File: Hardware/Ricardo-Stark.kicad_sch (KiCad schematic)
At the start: 40 parts, among them J1 RBUS, U1 ESP32-S3, Y1 R940000171

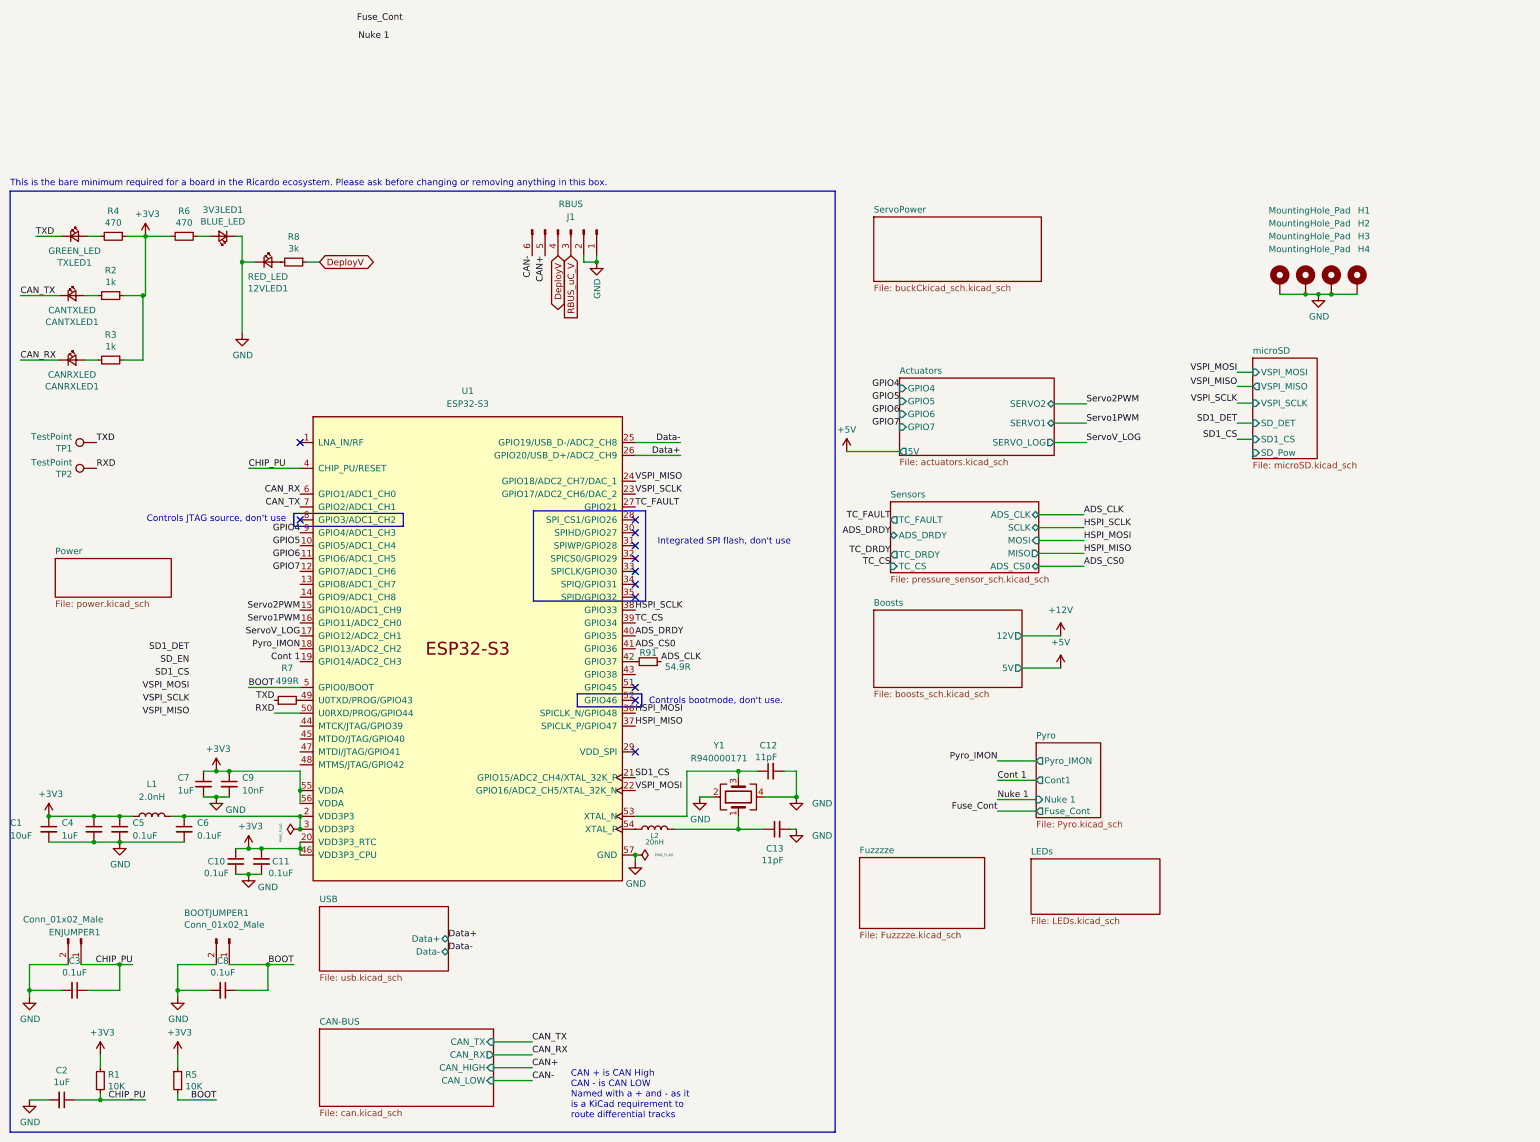
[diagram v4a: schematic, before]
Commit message: Routed Switch and Servo driver subsystems
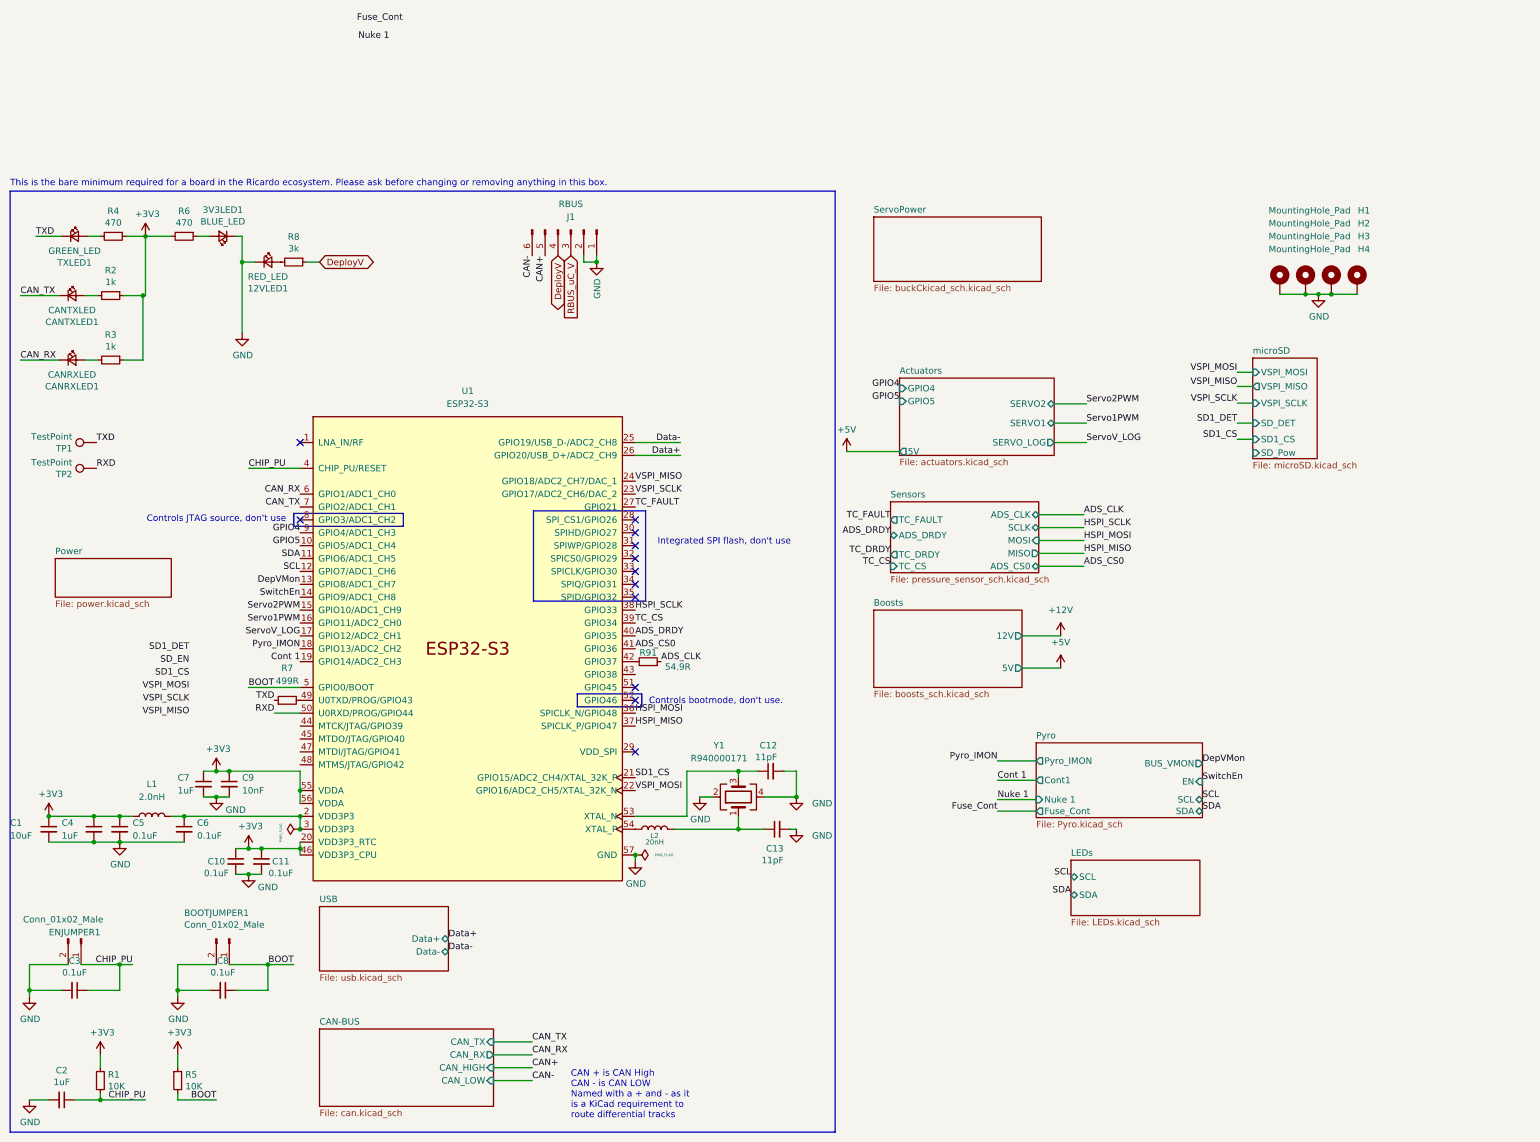
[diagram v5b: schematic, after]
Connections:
- net DepVMon: now reaches U1.13 (GPIO8/ADC1_CH7)
- net SwitchEn: now reaches U1.14 (GPIO9/ADC1_CH8)
- net GPIO6 renamed SDA
- net GPIO7 renamed SCL
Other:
- removed sheet Fuzzzze
- sheet Actuators ports: added none; removed GPIO6, GPIO7
- sheet LEDs ports: added SCL, SDA; removed none
- sheet Pyro ports: added BUS_VMON, EN, SCL, SDA; removed none
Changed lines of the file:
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@@
 		)
 	)
+	(label "SwitchEn"
+		(at 247.65 129.032 0)
+		(effects
+			(font
+				(size 1.27 1.27)
+			)
+			(justify left bottom)
+		)
+	)
 	(label "Nuke 1"
 		(at 207.264 132.588 0)
@@
 		)
 	)
+	(label "DepVMon"
+		(at 69.85 90.17 180)
+		(effects
+			(font
+				(size 1.27 1.27)
+			)
+			(justify right bottom)
+		)
+	)
 	(label "GPIO4"
 		(at 187.96 51.562 180)
@@
 		)
 	)
+	(label "SCL"
+		(at 247.65 132.588 0)
+		(effects
+			(font
+				(size 1.27 1.27)
+			)
+			(justify left bottom)
+		)
+	)
 	(label "VSPI_MISO"
 		(at 135.89 69.85 0)
@@
 		)
 	)
+	(label "SCL"
+		(at 221.742 147.828 180)
+		(effects
+			(font
+				(size 1.27 1.27)
+			)
+			(justify right bottom)
+		)
+	)
 	(label "HSPI_SCLK"
 		(at 135.89 95.25 0)
@@
 		)
 	)
-	(label "GPIO7"
-		(at 187.96 59.182 180)
-		(effects
-			(font
-				(size 1.27 1.27)
-			)
-			(justify right bottom)
-		)
-	)
 	(label "Data-"
 		(at 99.06 162.56 0)
@@
 		)
 	)
+	(label "SDA"
+		(at 221.742 151.384 180)
+		(effects
+			(font
+				(size 1.27 1.27)
+			)
+			(justify right bottom)
+		)
+	)
 	(label "TC_DRDY"
 		(at 186.182 84.328 180)
@@
 		)
 	)
+	(label "SDA"
+		(at 69.85 85.09 180)
+		(effects
+			(font
+				(size 1.27 1.27)
+			)
+			(justify right bottom)
+		)
+	)
 	(label "TC_FAULT"
 		(at 135.89 74.93 0)
@@
 		)
 	)
+	(label "SwitchEn"
+		(at 69.85 92.71 180)
+		(effects
+			(font
+				(size 1.27 1.27)
+			)
+			(justify right bottom)
+		)
+	)
 	(label "CAN_TX"
 		(at 14.732 33.274 0)
@@
 		)
 	)
+	(label "SCL"
+		(at 69.85 87.63 180)
+		(effects
+			(font
+				(size 1.27 1.27)
+			)
+			(justify right bottom)
+		)
+	)
 	(label "SD1_DET"
 		(at 254.508 58.42 180)
@@
 		)
 	)
-	(label "GPIO7"
-		(at 69.85 87.63 180)
-		(effects
-			(font
-				(size 1.27 1.27)
-			)
-			(justify right bottom)
-		)
-	)
 	(label "VSPI_SCLK"
 		(at 254.508 54.483 180)
@@
 		)
 	)
-	(label "GPIO6"
-		(at 187.96 56.642 180)
+	(label "ServoV_LOG"
+		(at 224.79 62.23 0)
 		(effects
 			(font
 				(size 1.27 1.27)
 			)
-			(justify right bottom)
+			(justify left bottom)
 		)
 	)
-	(label "ServoV_LOG"
-		(at 224.79 62.23 0)
+	(label "VSPI_MOSI"
+		(at 135.89 130.81 0)
 		(effects
 			(font
@@
 		)
 	)
-	(label "VSPI_MOSI"
-		(at 135.89 130.81 0)
+	(label "DepVMon"
+		(at 247.65 125.476 0)
 		(effects
 			(font
@@
 		)
 	)
-	(label "GPIO6"
-		(at 69.85 85.09 180)
+	(label "SDA"
+		(at 247.65 134.874 0)
 		(effects
 			(font
 				(size 1.27 1.27)
 			)
-			(justify right bottom)
+			(justify left bottom)
 		)
 	)
@@
 	(sheet
 		(at 214.884 121.412)
-		(size 12.7 14.732)
+		(size 32.766 14.732)
 		(exclude_from_sim no)
 		(in_bom yes)
@@
 			)
 		)
+		(pin "BUS_VMON" output
+			(at 247.65 125.476 0)
+			(effects
+				(font
+					(size 1.27 1.27)
+				)
+				(justify right)
+			)
+		)
+		(pin "EN" input
+			(at 247.65 129.032 0)
+			(effects
+				(font
+					(size 1.27 1.27)
+				)
+				(justify right)
+			)
+		)
+		(pin "SCL" bidirectional
+			(at 247.65 132.588 0)
+			(effects
+				(font
+					(size 1.27 1.27)
+				)
+				(justify right)
+			)
+		)
+		(pin "SDA" bidirectional
+			(at 247.65 134.874 0)
+			(effects
+				(font
+					(size 1.27 1.27)
+				)
+				(justify right)
+			)
+		)
 		(instances
 			(project "Ricardo-Stark"
@@
 	)
 	(sheet
-		(at 213.868 144.272)
+		(at 221.742 144.526)
 		(size 25.4 10.922)
 		(exclude_from_sim no)
@@
 		)
 		(property "Sheetname" "LEDs"
-			(at 213.868 143.5604 0)
+			(at 221.742 143.8144 0)
 			(effects
 				(font
@@
 		)
 		(property "Sheetfile" "LEDs.kicad_sch"
-			(at 213.868 155.7786 0)
+			(at 221.742 156.0326 0)
 			(effects
 				(font
@@
 			)
 		)
+		(pin "SCL" bidirectional
+			(at 221.742 147.828 180)
+			(effects
+				(font
+					(size 1.27 1.27)
+				)
+				(justify left)
+			)
+		)
+		(pin "SDA" bidirectional
+			(at 221.742 151.384 180)
+			(effects
+				(font
+					(size 1.27 1.27)
+				)
+				(justify left)
+			)
+		)
 		(instances
 			(project "Ricardo-Stark"
@@
 			)
 		)
-		(pin "GPIO6" input
-			(at 187.96 56.642 180)
-			(effects
-				(font
-					(size 1.27 1.27)
-				)
-				(justify left)
-			)
-		)
-		(pin "GPIO7" input
-			(at 187.96 59.182 180)
-			(effects
-				(font
-					(size 1.27 1.27)
-				)
-				(justify left)
-			)
-		)
 		(instances
 			(project "Ricardo-Stark"
@@
 				)
 			)
-		)
-	)
-	(sheet
-		(at 180.086 144.018)
-		(size 24.638 13.97)
-		(exclude_from_sim no)
-		(in_bom yes)
-		(on_board yes)
-		(dnp no)
-		(fields_autoplaced yes)
-		(stroke
-			(width 0.1524)
-			(type solid)
-		)
-		(fill
-			(color 0 0 0 0.0000)
-		)
-		(property "Sheetname" "Fuzzzze"
-			(at 180.086 143.3064 0)
-			(effects
-				(font
-					(size 1.27 1.27)
-				)
-				(justify left bottom)
-			)
-		)
-		(property "Sheetfile" "Fuzzzze.kicad_sch"
-			(at 180.086 158.5726 0)
-			(effects
-				(font
-					(size 1.27 1.27)
-				)
-				(justify left top)
-			)
-		)
-		(instances
-			(project "Ricardo-Stark"
-				(path "/7db990e4-92e1-4f99-b4d2-435bbec1ba83"
-					(page "12")
-				)
-			)

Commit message: Added actuators and I2C bus
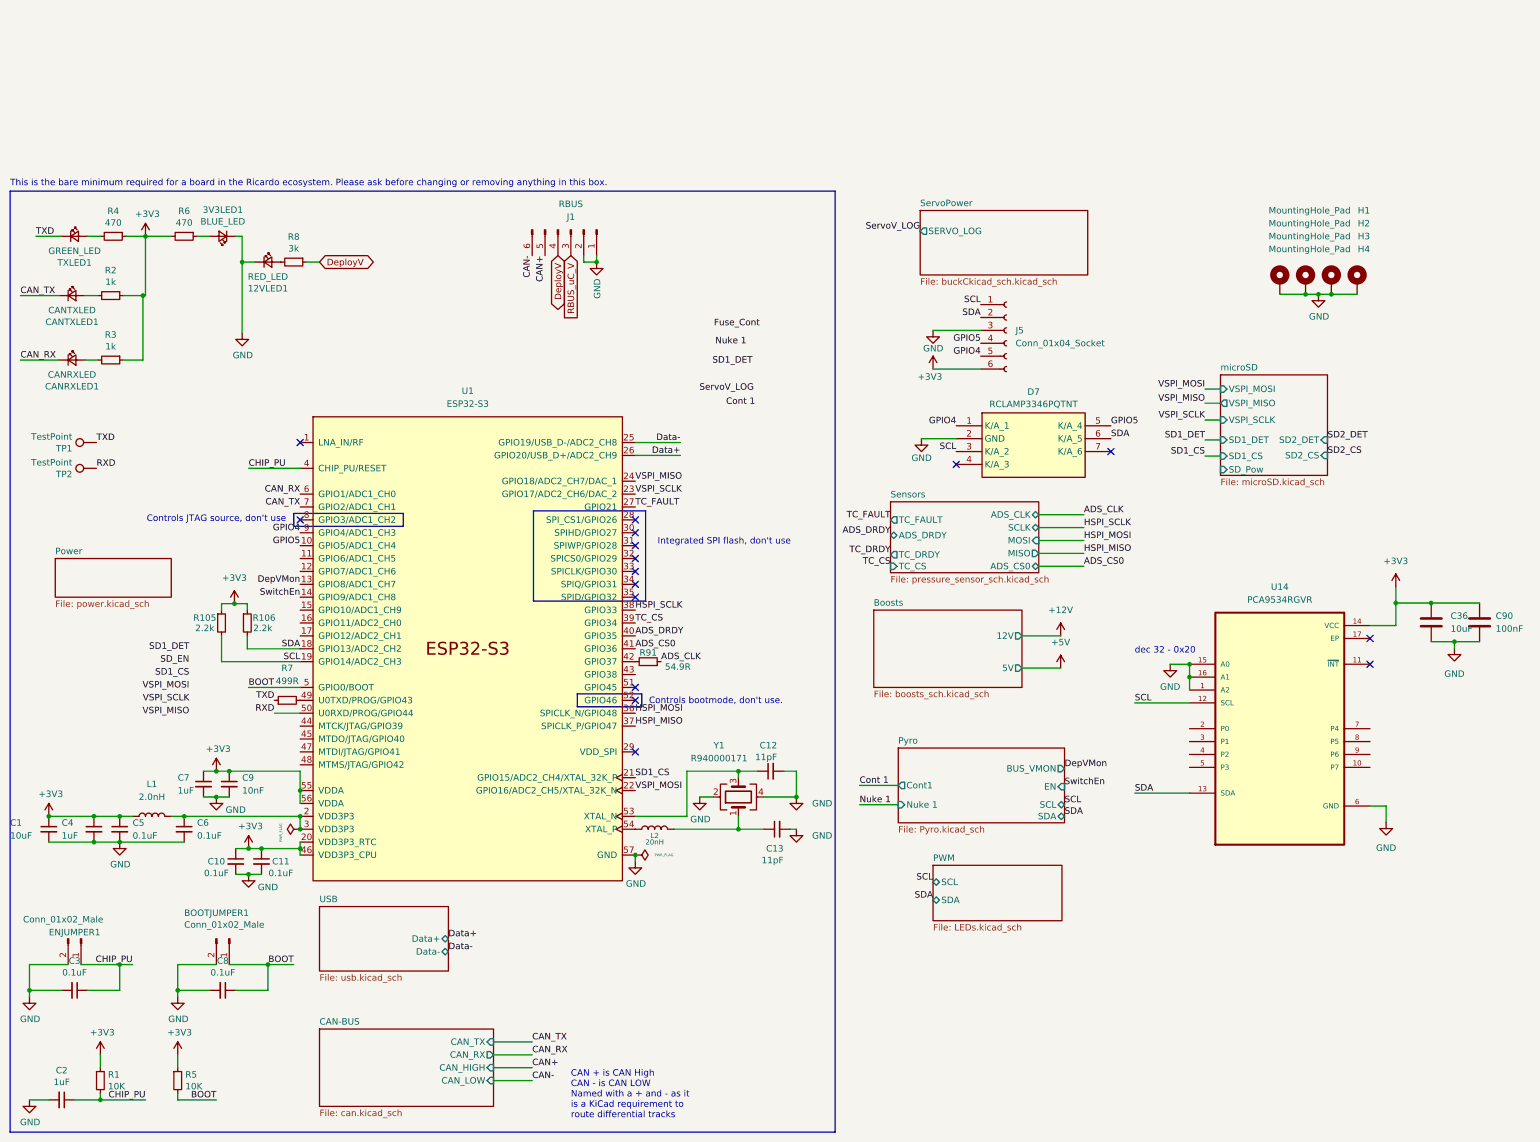
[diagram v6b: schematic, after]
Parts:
- added C36: 10uF, Capacitor_SMD:C_0402_1005Metric, symbol Device:C
- added C90: 100nF, Capacitor_SMD:C_0402_1005Metric, symbol Device:C
- added D7: RCLAMP3346PQTNT, iclr:RCLAMP3346PQTNT, symbol iclr:RCLAMP3346PQTNT
- added J5: Conn_01x04_Socket, Connector_PinHeader_2.54mm:PinHeader_1x06_P2.54mm_Vertical, symbol Connector:Conn_01x06_Socket
- added R105, R106: 2.2k, Resistor_SMD:R_0402_1005Metric, symbol Device:R_Small
- added U14: PCA9534RGVR, iclr:QFN65P400X400X100-17N, symbol iclr:PCA9534RGVR
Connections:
- net Pyro_IMON is gone; now on net SDA: U1.18 (GPIO13/ADC2_CH2)
- net +3V3: now also C36.1, C90.1, J5.6 (Pin_6), R105.1, R106.1, U14.14 (VCC)
- net Cont 1: no longer U1.19 (GPIO14/ADC2_CH3)
- net GND: now also C36.2, C90.2, D7.2 (GND), J5.3 (Pin_3), U14.1 (A2), U14.15 (A0), U14.16 (A1), U14.6 (GND)
- net GPIO4: now also D7.1 (K/A_1), J5.5 (Pin_5)
- net GPIO5: now also D7.5 (K/A_4), J5.4 (Pin_4)
- net SCL: now also U1.19 (GPIO14/ADC2_CH3), D7.3 (K/A_2), J5.1 (Pin_1), R105.2, U14.12 (SCL); no longer U1.12 (GPIO7/ADC1_CH6)
- net SDA: now also D7.6 (K/A_5), J5.2 (Pin_2), R106.2, U14.13 (SDA); no longer U1.11 (GPIO6/ADC1_CH5)
- net ServoV_LOG: no longer U1.17 (GPIO12/ADC2_CH1)
- net Servo1PWM: no longer names the net of U1.16 (GPIO11/ADC2_CH0)
- net Servo2PWM: no longer names the net of U1.15 (GPIO10/ADC1_CH9)
- no-connect marks 12 -> 16
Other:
- sheet LEDs renamed PWM
- removed sheet Actuators
- sheet Pyro ports: added none; removed Fuse_Cont, Pyro_IMON
- sheet ServoPower ports: added SERVO_LOG; removed none
- sheet microSD ports: added SD1_DET, SD2_CS, SD2_DET; removed SD_DET
- note added: "dec 32 - 0x20"

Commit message: Almost done
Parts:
- removed J5: Conn_01x04_Socket, Connector_PinHeader_2.54mm:PinHeader_1x06_P2.54mm_Vertical, symbol Connector:Conn_01x06_Socket
- added J11: Conn_01x08_Socket, Connector_PinHeader_2.54mm:PinHeader_2x04_P2.54mm_Vertical, symbol Connector:Conn_01x08_Socket
- added J5: Conn_01x03_Socket, Connector_PinHeader_2.54mm:PinHeader_1x03_P2.54mm_Vertical, symbol Connector:Conn_01x03_Socket
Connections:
- net DepVMon is gone; now on net ServoV_LOG: U1.13 (GPIO8/ADC1_CH7)
- net +3V3: now also J11.7 (Pin_7), J11.8 (Pin_8)
- net CAN_RX: now also U1.15 (GPIO10/ADC1_CH9); no longer U1.6 (GPIO1/ADC1_CH0)
- net CAN_TX: now also U1.16 (GPIO11/ADC2_CH0); no longer U1.7 (GPIO2/ADC1_CH1)
- net GND: now also J11.1 (Pin_1), J11.2 (Pin_2), J5.1 (Pin_1)
- net GPIO4: now also D7.6 (K/A_5), J11.4 (Pin_4); no longer D7.1 (K/A_1)
- net GPIO5: now also D7.3 (K/A_2), J11.3 (Pin_3); no longer D7.5 (K/A_4)
- net Nuke 1: now also U14.4 (P2)
- net SCL: now also D7.4 (K/A_3), U1.12 (GPIO7/ADC1_CH6), J5.2 (Pin_2); no longer D7.3 (K/A_2), U1.19 (GPIO14/ADC2_CH3)
- net SD1_DET: now also U14.7 (P4)
- net SD2_CS: now also U1.17 (GPIO12/ADC2_CH1)
- net SD2_DET: now also U14.8 (P5)
- net SDA: now also D7.7 (K/A_6), U1.11 (GPIO6/ADC1_CH5), J5.3 (Pin_3); no longer D7.6 (K/A_5), U1.18 (GPIO13/ADC2_CH2)
- net SwitchEn: now also U14.3 (P1); no longer U1.14 (GPIO9/ADC1_CH8)
- net PyroCont: now reaches U14.5 (P3)
- new net GPIO1: D7.1 (K/A_1), J11.6 (Pin_6), U1.6 (GPIO1/ADC1_CH0)
- new net GPIO2: D7.5 (K/A_4), J11.5 (Pin_5), U1.7 (GPIO2/ADC1_CH1)
- new net PyroV: U1.14 (GPIO9/ADC1_CH8)
- new net Servo0: U1.19 (GPIO14/ADC2_CH3)
- new net Servo1: U1.18 (GPIO13/ADC2_CH2)
- no-connect marks 16 -> 14
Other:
- sheet PWM ports: added Servo0, Servo1; removed none
- sheet Pyro ports: added PyroVMON; removed BUS_VMON
- moved on the sheet: R105, R106

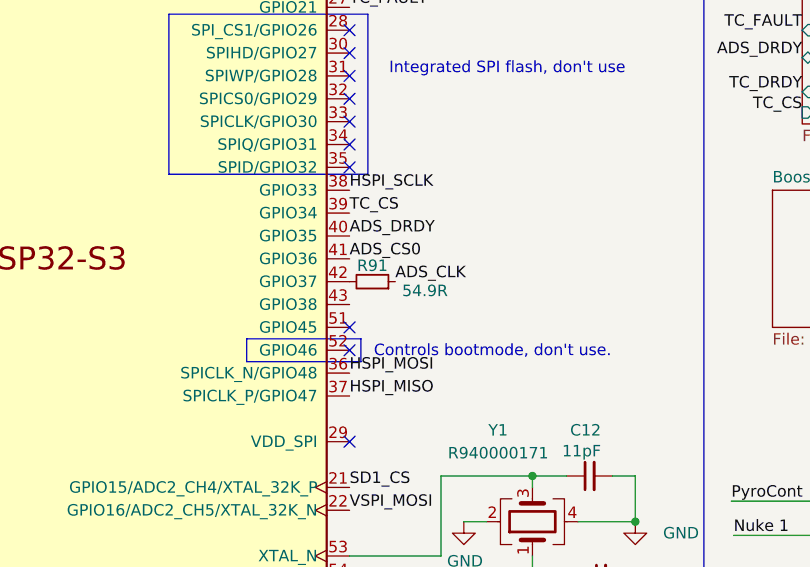
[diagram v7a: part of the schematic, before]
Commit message: Fixed all DRC Errors
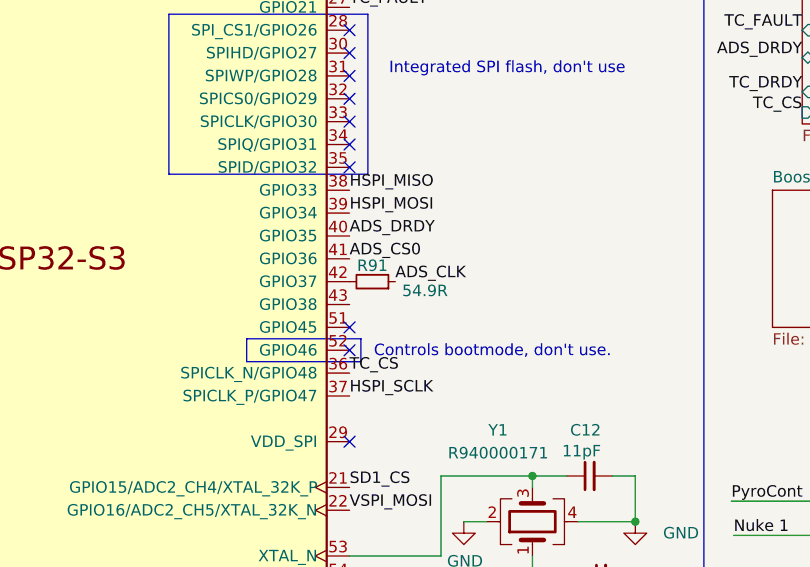
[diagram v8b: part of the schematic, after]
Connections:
- net HSPI_MISO: now also U1.38 (GPIO33); no longer U1.37 (SPICLK_P/GPIO47)
- net HSPI_MOSI: now also U1.39 (GPIO34); no longer U1.36 (SPICLK_N/GPIO48)
- net HSPI_SCLK: now also U1.37 (SPICLK_P/GPIO47); no longer U1.38 (GPIO33)
- net TC_CS: now also U1.36 (SPICLK_N/GPIO48); no longer U1.39 (GPIO34)
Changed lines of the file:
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@@
 	)
 	(label "HSPI_SCLK"
-		(at 135.89 95.25 0)
+		(at 135.89 118.11 0)
 		(effects
 			(font
@@
 	)
 	(label "TC_CS"
-		(at 135.89 97.79 0)
+		(at 135.89 115.57 0)
 		(effects
 			(font
@@
 	)
 	(label "HSPI_MISO"
-		(at 135.89 118.11 0)
+		(at 135.89 95.25 0)
 		(effects
 			(font
@@
 	)
 	(label "HSPI_MOSI"
-		(at 135.89 115.57 0)
-		(effects
-			(font
+		(at 135.89 97.79 0)
+		(effects
+			(font
